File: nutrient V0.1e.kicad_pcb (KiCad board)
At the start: 2 copper layers, 99.1 x 71.1 mm, 76 parts, among them J1 Conn_01x04_Female, J10 Conn_01x01_Male, J2 Conn_01x04_Female, J3 Conn_01x04_Female, J4 Conn_01x04_Female, J5 Conn_01x04_Female, J6 Conn_01x04_Female, J7 Conn_01x03_Male, J8 Conn_01x03_Male, J9 Conn_01x01_Male, P1 SolderJumper_2_Open, P2 SolderJumper_2_Open, Q1 Q_NMOS_DGS, Q10 Q_NMOS_DGS, Q2 Q_NMOS_DGS, Q3 Q_NMOS_DGS, Q4 Q_NMOS_DGS, Q5 Q_NMOS_DGS, Q6 Q_NMOS_DGS, Q7 Q_NMOS_DGS, Q8 2N3904, U1 23LC512, U2 DS1307+, Y1 Crystal_Small

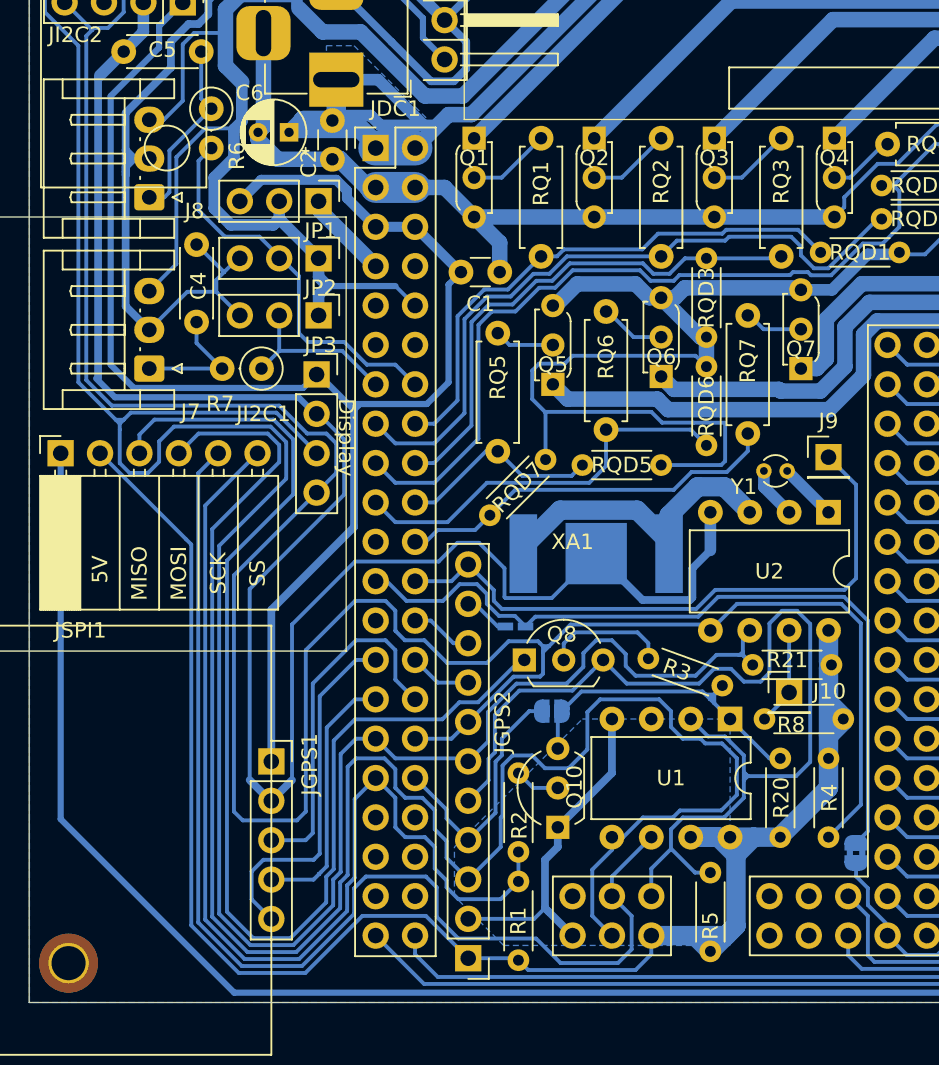
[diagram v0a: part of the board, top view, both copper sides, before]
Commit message: Minor track changes
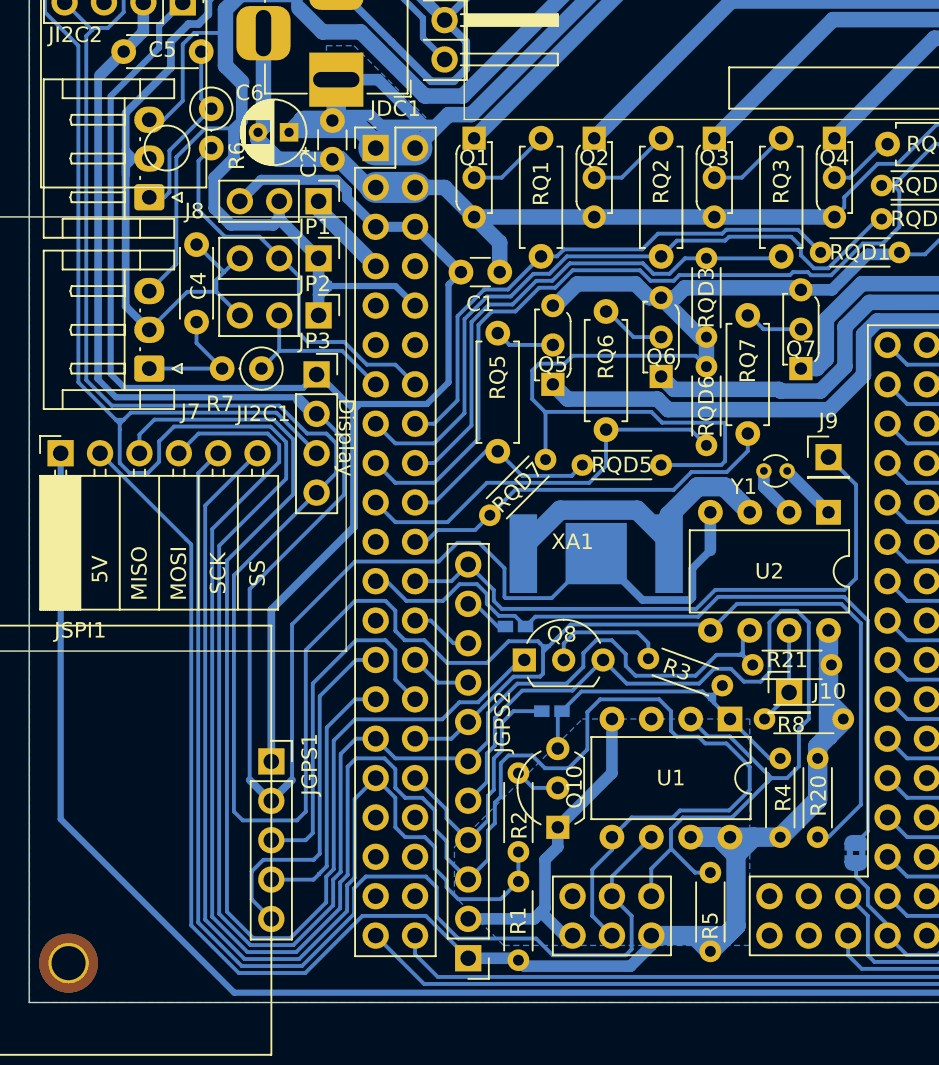
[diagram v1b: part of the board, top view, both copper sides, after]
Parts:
- P2: value SolderJumper_2_Open -> SolderJumper_2_Bridged
- SSRAM1: footprint Jumper:SolderJumper-2_P1.3mm_Open_RoundedPad1.0x1.5mm -> Jumper:SolderJumper-2_P1.3mm_Open_RoundedPad0.5x0.75mm
- moved R20 0.70 mm to (150.4, 95.2)
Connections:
- net /SS_RAM renamed /SS_AUX
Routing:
- net /VIN: track 206.4 -> 208.1 mm
- net /MOSI: track 120.9 -> 122.3 mm
- net /SS_AUX: track 16.2 -> 16.8 mm
- net /5V3: track 111.0 -> 110.5 mm

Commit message: Minor layout change
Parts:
- moved P2 0.38 mm to (152.5, 96.3)
- moved P1 0.13 mm to (130.9, 81.8)

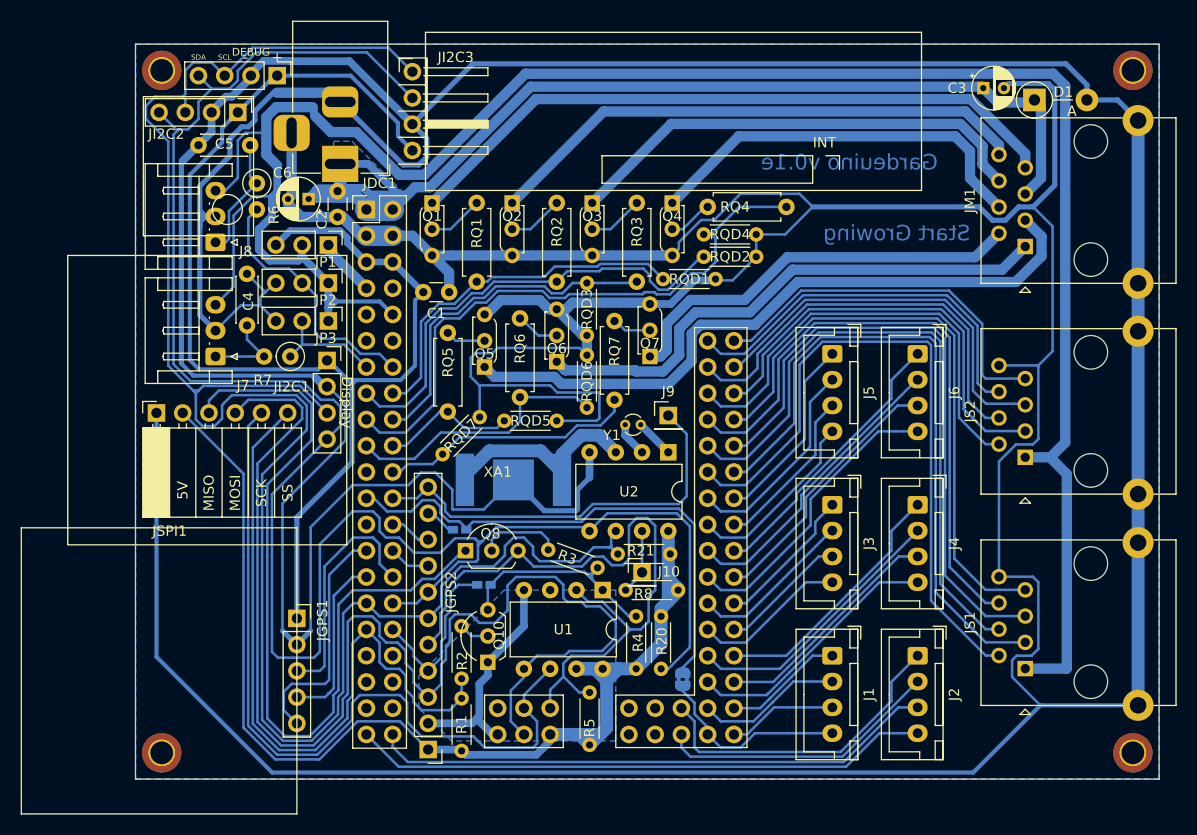
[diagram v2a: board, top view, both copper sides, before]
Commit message: External header changes
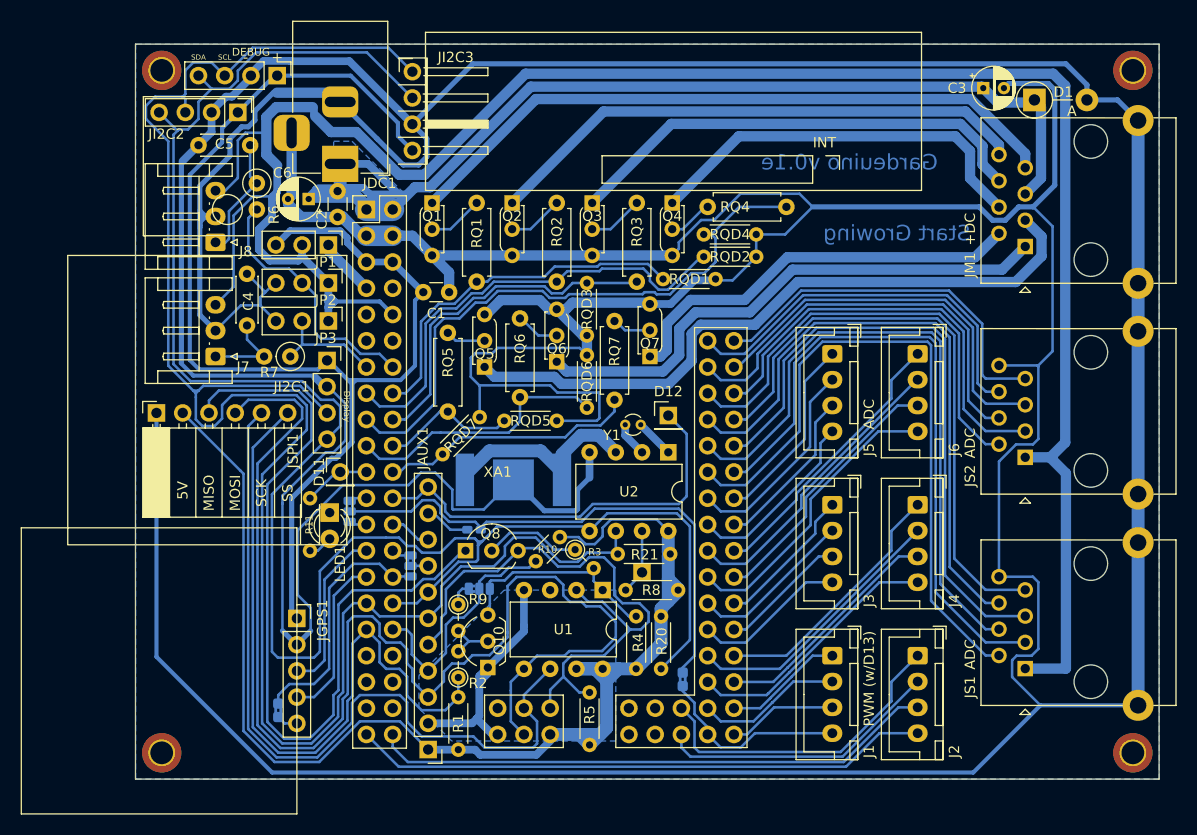
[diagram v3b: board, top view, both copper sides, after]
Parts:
- removed SSRAM1: SolderJumper_2_Open, Jumper:SolderJumper-2_P1.3mm_Open_RoundedPad0.5x0.75mm
- added D11: Conn_01x01_Male, Connector_PinHeader_2.54mm:PinHeader_1x01_P2.54mm_Vertical, F.Cu at (119.4, 76.2)
- added JP4: SolderJumper_3_Bridged12, Library:SolderJumper-3_P1.3mm_Bridged2Bar12_RoundedPad1.0x1.5mm_narrow, B.Cu at (132.8, 87.5)
- added JP5: SolderJumper_3_Bridged12, Jumper:SolderJumper-3_P1.3mm_Bridged2Bar12_RoundedPad1.0x1.5mm, B.Cu at (126.2, 85.3)
- added JP6: SolderJumper_3_Bridged12, Library:SolderJumper-3_P1.3mm_Bridged2Bar12_RoundedPad1.0x1.5mm_narrow, B.Cu at (120.3, 80.0)
- added LED1: LED, LED_THT:LED_D3.0mm, F.Cu at (118.4, 80.1)
- added P3: SolderJumper_2_Bridged, Library:SolderJumper-2_P1.3mm_Bridged2Bar_RoundedPad1.0x1.5mm_narrow, B.Cu at (113.4, 99.3)
- added R10: 4k7, Resistor_THT:R_Axial_DIN0204_L3.6mm_D1.6mm_P5.08mm_Horizontal, F.Cu at (141.0, 82.1)
- added R11: R, Resistor_THT:R_Axial_DIN0204_L3.6mm_D1.6mm_P5.08mm_Horizontal, F.Cu at (116.5, 78.7)
- added R9: 4k7, Resistor_THT:R_Axial_DIN0204_L3.6mm_D1.6mm_P2.54mm_Vertical, F.Cu at (130.8, 89.0)
- R2, R3: footprint Resistor_THT:R_Axial_DIN0204_L3.6mm_D1.6mm_P5.08mm_Horizontal -> Resistor_THT:R_Axial_DIN0204_L3.6mm_D1.6mm_P2.54mm_Vertical
- moved R2 4.98 mm to (130.8, 96.1), turned to 90 degrees
- moved R3 2.60 mm to (142.1, 83.7), turned to -45 degrees
- moved P1 1.40 mm to (132.3, 81.8)
- moved Q10 0.51 mm to (133.7, 95.1)
- moved R1 0.34 mm to (130.8, 103.1)
- renumbered J9 to D12, JGPS2 to JAUX1, J10 to JSQW1
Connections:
- net /AD0 renamed /OPT_EXT
- net /D14 renamed /TX
- net /INT4 renamed /D12
- net Net-(Q10-Pad3) renamed /SS_RAM
- JAUX1 pad 8: /D16 -> /XCL
- P1 pad 2: /D13 -> /OPT
- P2 pad 2: /D13 -> /OPT
- R2 pad 1: Net-(Q10-Pad2) -> /SS_MMC
- R2 pad 2: /SS_MMC -> Net-(Q10-Pad2)
- U1 pad 3: Net-(U1-Pad3) -> unconnected-(U1-Pad3)
- XA1 pad 3V2: Net-(XA1-Pad3V2) -> unconnected-(XA1-Pad3V2)
- XA1 pad D0: Net-(XA1-PadD0) -> unconnected-(XA1-PadD0)
- XA1 pad D1: Net-(XA1-PadD1) -> unconnected-(XA1-PadD1)
- XA1 pad D11: Net-(XA1-PadD11) -> /D11
- XA1 pad D15: Net-(XA1-PadD15) -> /RX
- XA1 pad D17: /PPS -> /GPSRX
- XA1 pad D18: /GPSRX -> /INT
- XA1 pad D24: Net-(XA1-PadD24) -> unconnected-(XA1-PadD24)
- XA1 pad D25: Net-(XA1-PadD25) -> unconnected-(XA1-PadD25)
- XA1 pad D26: Net-(XA1-PadD26) -> unconnected-(XA1-PadD26)
- XA1 pad D27: Net-(XA1-PadD27) -> unconnected-(XA1-PadD27)
- XA1 pad D28: Net-(XA1-PadD28) -> unconnected-(XA1-PadD28)
- XA1 pad D29: Net-(XA1-PadD29) -> unconnected-(XA1-PadD29)
- XA1 pad D50: Net-(XA1-PadD50) -> unconnected-(XA1-PadD50)
- XA1 pad D51: Net-(XA1-PadD51) -> unconnected-(XA1-PadD51)
- XA1 pad D52: Net-(XA1-PadD52) -> unconnected-(XA1-PadD52)
- XA1 pad D53: Net-(XA1-PadD53) -> unconnected-(XA1-PadD53)
- XA1 pad RST1: Net-(XA1-PadRST1) -> unconnected-(XA1-PadRST1)
- XA1 pad RST2: Net-(XA1-PadRST2) -> unconnected-(XA1-PadRST2)
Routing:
- net /OPT: track 0.00 -> 52.2 mm
- net /D13: track 50.5 -> 1.98 mm
- net /INT: track 0.00 -> 24.0 mm
- net /PPS: track 23.2 -> 2.06 mm
- net /5V3: track 110.5 -> 123.6 mm
- net /MISO: track 68.1 -> 58.3 mm
- net /SS_AUX: track 16.8 -> 23.8 mm
- net /GPSRX: track 23.0 -> 16.1 mm
- net /D11: track 0.00 -> 6.51 mm
- net /SDA: track 185.3 -> 181.2 mm
- net GND: track 721.2 -> 724.2 mm
- net Net-(LED1-Pad2): track 0.00 -> 2.38 mm
- net /SS_INV: track 0.00 -> 2.32 mm
- net /GND3: track 21.9 -> 24.1 mm
- net /D16: track 4.03 -> 1.92 mm
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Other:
- net class Default removed
- board text added: "+DC"
- board text added: "ADC"
- board text added: "D12 PWM"
- board text added: "D13 PWM"
- board text added: "D15 rx"
- board text added: "EXT"
- board text added: "EXT_enable"
- board text added: "GND"
- board text added: "GPSRX"
- board text added: "GPSTX"
- board text added: "INT_disable"
- board text added: "OPT"
- board text added: "OPT_disable"
- board text added: "PPS"
- board text added: "PWM (w/D13)"
- board text added: "SQW"
- board text added: "SS_AUX"
- board text added: "SS_MMC"
- board text added: "SS_aux !SS_*"
- board text added: "XCL int"
- board text added: "XDA TX"

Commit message: Trace changes, GND loop fixes
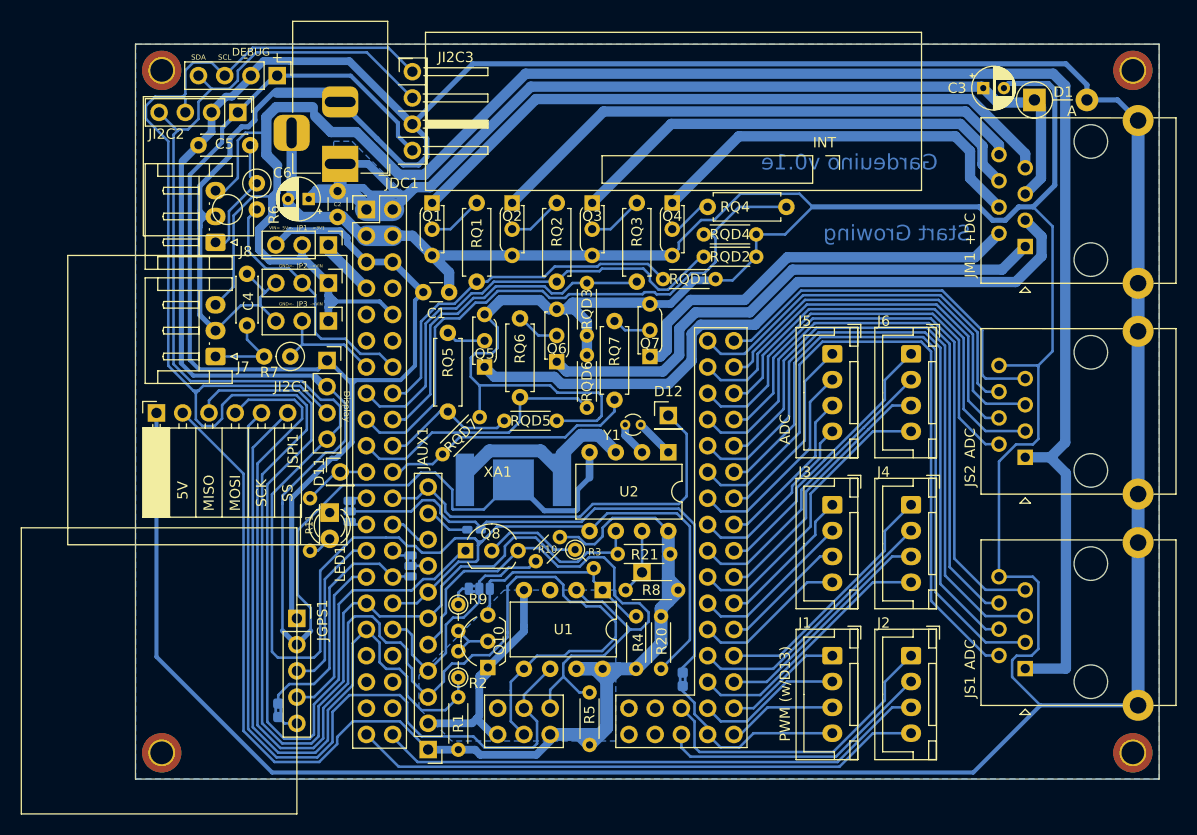
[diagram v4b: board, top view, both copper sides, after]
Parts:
- moved J2 0.63 mm to (174.6, 94.0)
- moved J4 0.63 mm to (174.6, 79.4)
- moved J6 0.63 mm to (174.6, 64.8)
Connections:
- net /MISO renamed /D50
- net /MOSI renamed /D51
- net /SCK renamed /D52
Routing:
- net GND: track 724.2 -> 719.1 mm
- net /D30: track 54.8 -> 53.6 mm
- net Net-(J2-Pad1): track 31.1 -> 30.3 mm
- net Net-(J4-Pad2): track 26.4 -> 25.7 mm
- net /D31: track 56.0 -> 55.3 mm
- net Net-(J4-Pad1): track 24.9 -> 24.3 mm
- net Net-(J2-Pad2): track 27.5 -> 26.9 mm
- net Net-(J4-Pad4): track 25.4 -> 24.7 mm
- net /D52: track 76.0 -> 76.6 mm
- net Net-(J4-Pad3): track 22.8 -> 22.2 mm
- net /5V3: track 123.6 -> 124.1 mm
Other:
- board text added: "->3V3"
- board text added: "->VIN"
- board text added: "5V<-"
- board text added: "GND<-"
- board text added: "VIN="
- board text added: "ss_aux !SS_*"
- board text removed: "SS_aux !SS_*"
